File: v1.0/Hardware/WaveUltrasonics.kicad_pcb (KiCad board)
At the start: 2 copper layers, 300 x 155 mm, 196 parts, among them J1 MAINS_IN, J2 Conn_02x08_Counter_Clockwise, J3 TRANSDUCER, J4 FAN, Q1 IXXH80N65B4H1, Q10 BC556, Q11 BC546, Q12 BC556, Q13 BC546, Q14 BC556, Q15 MMBT3904, Q16 MMBT3904, Q17 MMBT3904, Q2 IXXH80N65B4H1, Q3 IXXH80N65B4H1, Q4 IXXH80N65B4H1, Q5 BC546, Q6 BC556, Q7 BC546, Q8 BC556, Q9 BC546, T1 Transformer_1P_1S, T2 Transformer_1P_2S, T3 Transformer_1P_2S, T4 Transformer_1P_2S, U1 4N39, U10 HCPL-3120, U11 HCPL-3120, U12 OPA228, U13 L78L05_SOT89, U14 TLV1117-33, U2 4N39, U3 MCP6024, U4 ACPL-7900, U5 TL431LP, U6 AMS1117-5.0, U7 BLUEPILL_STM32F103, U8 HCPL-3120, U9 HCPL-3120

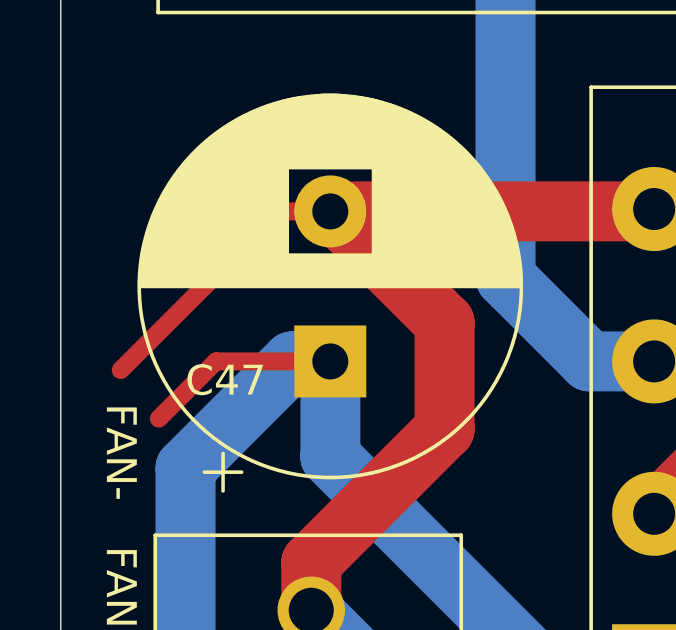
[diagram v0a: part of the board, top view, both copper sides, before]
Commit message: v1.1&v1.2 PCB addition.
#####v1.1#####
+Change of MCU; STM32F334C8T6 instead of STM32F103C8T6.
+Filtering 3rd order components of the square wave.
+Use  4 capacitors.
+Adapted to generic transformer(primary 6.4mH, secondary 14.4mH)
+Faster IGBT.

########v1.2#######
+Measures only PZT current and voltage.
+Differential inputs.
+Analog circuitry is capable of measuring four quadrant voltage, current and complex impedance.
+Half bridge configuration.
+Gate resistance of the IGBT's lowered.
+Only USART based touch panel can be connected; not conventional LCD.
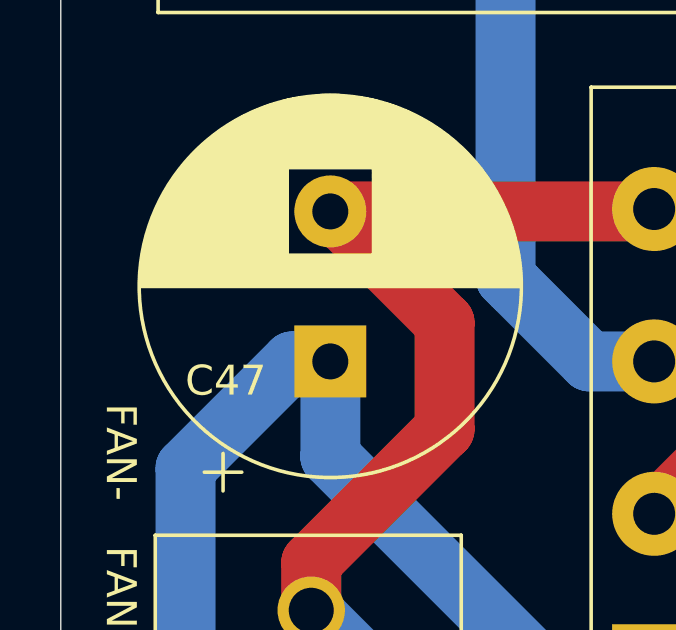
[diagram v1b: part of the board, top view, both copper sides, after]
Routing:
- net GND1: track 131.1 -> 122.0 mm
- net VEE: track 89.4 -> 82.9 mm
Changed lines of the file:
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@@
     (thickness 1.6)
     (drawings 74)
-    (tracks 1310)
+    (tracks 1306)
     (modules 196)
     (nets 119)
@@
     (pad_to_mask_clearance 0.05)
     (aux_axis_origin 0 0)
-    (visible_elements FFFFFF7F)
+    (visible_elements FFFFF77F)
     (pcbplotparams
       (layerselection 0x010f0_ffffffff)
@@
   (segment (start 64.77 142.24) (end 64.77 156.21) (width 0.6) (layer "B.Cu") (net 12))
   (segment (start 64.77 156.21) (end 65.405 156.845) (width 0.6) (layer "B.Cu") (net 12))
-  (segment (start 66.675 116.35525) (end 64.77 118.26025) (width 0.6) (layer "F.Cu") (net 12))
   (via (at 65.405 156.845) (size 1.25) (drill 0.8) (layers "F.Cu" "B.Cu") (net 12))
   (via (at 65.405 139.065) (size 1.25) (drill 0.8) (layers "F.Cu" "B.Cu") (net 12))
   (segment (start 63.5 158.75) (end 65.405 156.845) (width 0.6) (layer "F.Cu") (net 12))
-  (segment (start 63.5 116.643194) (end 68.787944 111.35525) (width 0.6) (layer "F.Cu") (net 10))
-  (segment (start 68.787944 111.35525) (end 70.485 111.35525) (width 0.6) (layer "F.Cu") (net 10))
   (segment (start 63.5 160.02) (end 63.5 158.75) (width 0.6) (layer "F.Cu") (net 12))
-  (segment (start 66.675 116.35525) (end 70.485 116.35525) (width 0.6) (layer "F.Cu") (net 12))
   (segment (start 70.875 159.63) (end 65.65 159.63) (width 0.6) (layer "B.Cu") (net 10))
   (segment (start 65.65 159.63) (end 63.5 157.48) (width 0.6) (layer "B.Cu") (net 10))
@@
     (connect_pads (clearance 0.508))
     (min_thickness 0.254)
-    (fill yes (thermal_gap 0.508) (thermal_bridge_width 0.508) (smoothing fillet) (radius 1.5))
+    (fill (thermal_gap 0.508) (thermal_bridge_width 0.508) (smoothing fillet) (radius 1.5))
     (polygon
       (pts
@@
     (connect_pads (clearance 1))
     (min_thickness 0.254)
-    (fill yes (thermal_gap 0.508) (thermal_bridge_width 0.508) (smoothing fillet) (radius 1.5))
+    (fill (thermal_gap 0.508) (thermal_bridge_width 0.508) (smoothing fillet) (radius 1.5))
     (polygon
       (pts
@@
     (connect_pads (clearance 1))
     (min_thickness 0.254)
-    (fill yes (thermal_gap 0.508) (thermal_bridge_width 0.508) (smoothing fillet) (radius 1.5))
+    (fill (thermal_gap 0.508) (thermal_bridge_width 0.508) (smoothing fillet) (radius 1.5))
     (polygon
       (pts
@@
     (connect_pads (clearance 1))
     (min_thickness 0.254)
-    (fill yes (thermal_gap 0.508) (thermal_bridge_width 0.508) (smoothing fillet) (radius 1.5))
+    (fill (thermal_gap 0.508) (thermal_bridge_width 0.508) (smoothing fillet) (radius 1.5))
     (polygon
       (pts
@@
     (connect_pads (clearance 1))
     (min_thickness 0.254)
-    (fill yes (thermal_gap 0.508) (thermal_bridge_width 0.508) (smoothing fillet) (radius 1.5))
+    (fill (thermal_gap 0.508) (thermal_bridge_width 0.508) (smoothing fillet) (radius 1.5))
     (polygon
       (pts
@@
     (connect_pads (clearance 1))
     (min_thickness 0.254)
-    (fill yes (thermal_gap 0.508) (thermal_bridge_width 0.508) (smoothing fillet) (radius 1.5))
+    (fill (thermal_gap 0.508) (thermal_bridge_width 0.508) (smoothing fillet) (radius 1.5))
     (polygon
       (pts
@@
     (connect_pads (clearance 1))
     (min_thickness 0.254)
-    (fill yes (thermal_gap 0.508) (thermal_bridge_width 0.508) (smoothing fillet) (radius 1.5))
+    (fill (thermal_gap 0.508) (thermal_bridge_width 0.508) (smoothing fillet) (radius 1.5))
     (polygon
       (pts
@@
     (connect_pads (clearance 1))
     (min_thickness 0.254)
-    (fill yes (thermal_gap 0.508) (thermal_bridge_width 0.508) (smoothing fillet) (radius 1.5))
+    (fill (thermal_gap 0.508) (thermal_bridge_width 0.508) (smoothing fillet) (radius 1.5))
     (polygon
       (pts
@@
     (connect_pads (clearance 1))
     (min_thickness 0.254)
-    (fill yes (thermal_gap 0.508) (thermal_bridge_width 0.508) (smoothing fillet) (radius 1.5))
+    (fill (thermal_gap 0.508) (thermal_bridge_width 0.508) (smoothing fillet) (radius 1.5))
     (polygon
       (pts
@@
     (connect_pads (clearance 1))
     (min_thickness 0.254)
-    (fill yes (thermal_gap 0.508) (thermal_bridge_width 0.508) (smoothing fillet) (radius 1.5))
+    (fill (thermal_gap 0.508) (thermal_bridge_width 0.508) (smoothing fillet) (radius 1.5))
     (polygon
       (pts
@@
     (connect_pads (clearance 1))
     (min_thickness 0.254)
-    (fill yes (thermal_gap 0.508) (thermal_bridge_width 0.508) (smoothing fillet) (radius 1.5))
+    (fill (thermal_gap 0.508) (thermal_bridge_width 0.508) (smoothing fillet) (radius 1.5))
     (polygon
       (pts
@@
     (connect_pads (clearance 1))
     (min_thickness 0.254)
-    (fill yes (thermal_gap 0.508) (thermal_bridge_width 0.508) (smoothing fillet) (radius 1.5))
+    (fill (thermal_gap 0.508) (thermal_bridge_width 0.508) (smoothing fillet) (radius 1.5))
     (polygon
       (pts
@@
     (connect_pads (clearance 0.508))
     (min_thickness 0.254)
-    (fill yes (thermal_gap 0.508) (thermal_bridge_width 0.508) (smoothing fillet) (radius 1.5))
+    (fill (thermal_gap 0.508) (thermal_bridge_width 0.508) (smoothing fillet) (radius 1.5))
     (polygon
       (pts
@@
     (connect_pads (clearance 0.508))
     (min_thickness 0.254)
-    (fill yes (thermal_gap 0.508) (thermal_bridge_width 0.508) (smoothing fillet) (radius 1.5))
+    (fill (thermal_gap 0.508) (thermal_bridge_width 0.508) (smoothing fillet) (radius 1.5))
     (polygon
       (pts
@@
     (connect_pads (clearance 0.508))
     (min_thickness 0.254)
-    (fill yes (thermal_gap 0.508) (thermal_bridge_width 0.508) (smoothing fillet) (radius 1.5))
+    (fill (thermal_gap 0.508) (thermal_bridge_width 0.508) (smoothing fillet) (radius 1.5))
     (polygon
       (pts
